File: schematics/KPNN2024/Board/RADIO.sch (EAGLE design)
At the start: 14 parts, among them J1 U.FL-R-SMT-1_10_, J2 U.FL-R-SMT-1_10_

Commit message: sdfghgfds
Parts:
- added C1: (no value), rcl:C-EUC0603
- added C2: ECAPECAP220, CanCubeSat:ECAPECAP220
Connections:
- net 3V3: no longer U$3.3.3V
- net 5V: now also C1.2, C2.1
- net GND: now also C1.1, C2.2
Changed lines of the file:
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@@
 <part name="R1" library="rcl" library_urn="urn:adsk.eagle:library:334" deviceset="R-US_" device="R0603" package3d_urn="urn:adsk.eagle:package:23555/3"/>
 <part name="R2" library="rcl" library_urn="urn:adsk.eagle:library:334" deviceset="R-US_" device="R0603" package3d_urn="urn:adsk.eagle:package:23555/3"/>
+<part name="C1" library="rcl" library_urn="urn:adsk.eagle:library:334" deviceset="C-EU" device="C0603" package3d_urn="urn:adsk.eagle:package:23616/2"/>
+<part name="C2" library="CanCubeSat" deviceset="ECAP" device="ECAP220"/>
 </parts>
 <sheets>
@@
 <attribute name="VALUE" x="143.51" y="83.058" size="1.778" layer="96"/>
 </instance>
+<instance part="C1" gate="G$1" x="53.34" y="83.82" smashed="yes">
+<attribute name="NAME" x="54.864" y="84.201" size="1.778" layer="95"/>
+<attribute name="VALUE" x="54.864" y="79.121" size="1.778" layer="96"/>
+</instance>
+<instance part="C2" gate="G$1" x="48.26" y="81.28" smashed="yes" rot="R180">
+<attribute name="NAME" x="47.244" y="80.645" size="1.778" layer="95" rot="R180"/>
+<attribute name="VALUE" x="47.244" y="85.471" size="1.778" layer="96" rot="R180"/>
+</instance>
 </instances>
 <busses>
@@
 <segment>
 <pinref part="U$3" gate="G$1" pin="GND"/>
-<wire x1="68.58" y1="83.82" x2="50.8" y2="83.82" width="0.1524" layer="91"/>
-<label x="50.8" y="83.82" size="1.778" layer="95"/>
+<wire x1="68.58" y1="83.82" x2="60.96" y2="83.82" width="0.1524" layer="91"/>
+<label x="55.88" y="86.36" size="1.778" layer="95"/>
+<pinref part="C1" gate="G$1" pin="1"/>
+<wire x1="53.34" y1="86.36" x2="60.96" y2="86.36" width="0.1524" layer="91"/>
+<wire x1="60.96" y1="86.36" x2="60.96" y2="83.82" width="0.1524" layer="91"/>
+<pinref part="C2" gate="G$1" pin="2"/>
+<wire x1="48.26" y1="86.36" x2="53.34" y2="86.36" width="0.1524" layer="91"/>
+<junction x="53.34" y="86.36"/>
 </segment>
 <segment>
@@
 </segment>
 <segment>
-<pinref part="U$3" gate="G$1" pin="3.3V"/>
-<wire x1="68.58" y1="73.66" x2="50.8" y2="73.66" width="0.1524" layer="91"/>
-<label x="50.8" y="73.66" size="1.778" layer="95"/>
-</segment>
-<segment>
 <pinref part="U$5" gate="G$1" pin="P$1"/>
 <wire x1="182.88" y1="83.82" x2="170.18" y2="83.82" width="0.1524" layer="91"/>
@@
 <segment>
 <pinref part="U$3" gate="G$1" pin="5V"/>
-<wire x1="68.58" y1="78.74" x2="50.8" y2="78.74" width="0.1524" layer="91"/>
-<label x="50.8" y="78.74" size="1.778" layer="95"/>
+<wire x1="68.58" y1="78.74" x2="53.34" y2="78.74" width="0.1524" layer="91"/>
+<label x="55.88" y="78.74" size="1.778" layer="95"/>
+<pinref part="C1" gate="G$1" pin="2"/>
+<pinref part="C2" gate="G$1" pin="1"/>
+<wire x1="48.26" y1="78.74" x2="53.34" y2="78.74" width="0.1524" layer="91"/>
+<junction x="53.34" y="78.74"/>
 </segment>
 <segment>

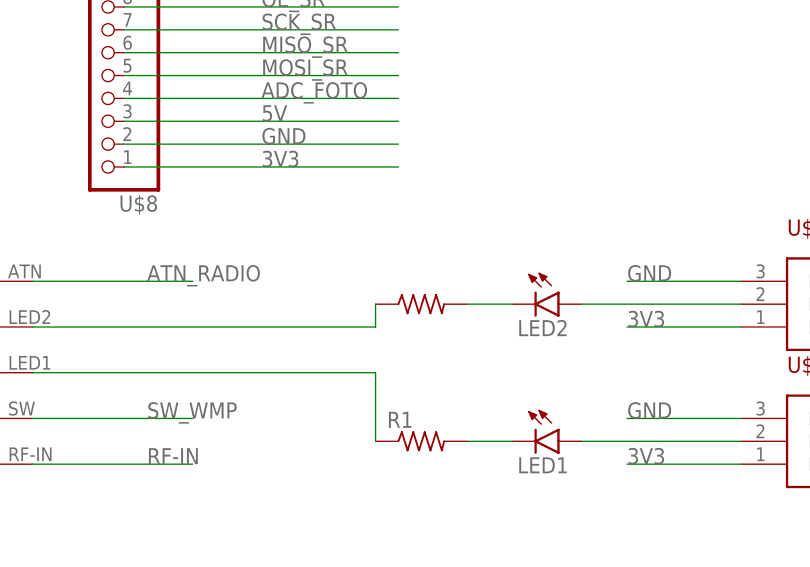
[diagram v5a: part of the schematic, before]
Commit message: добавлены стл корпусных деталей
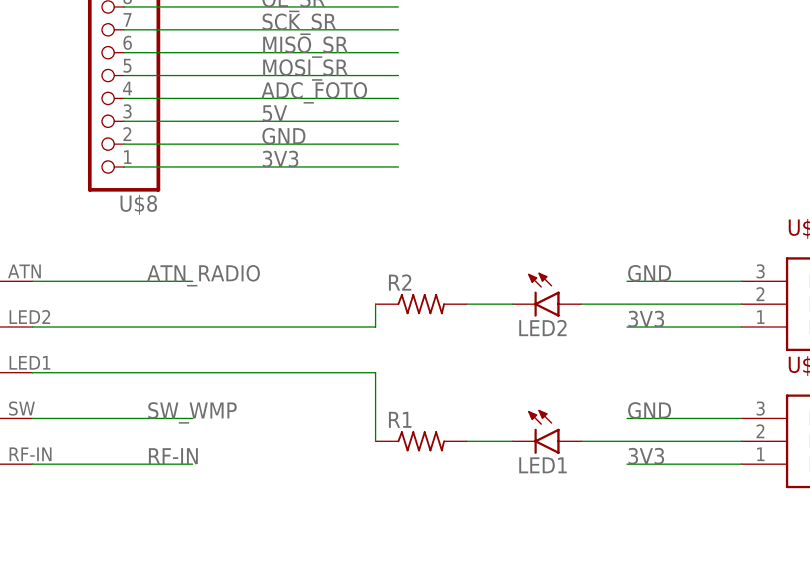
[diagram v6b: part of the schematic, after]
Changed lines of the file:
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@@
 <?xml version="1.0" encoding="utf-8"?>
 <!DOCTYPE eagle SYSTEM "eagle.dtd">
-<eagle version="9.6.0">
+<eagle version="9.6.2">
 <drawing>
 <settings>
@@
 </instance>
 <instance part="R2" gate="G$1" x="147.32" y="86.36" smashed="yes">
+<attribute name="NAME" x="143.51" y="87.8586" size="1.778" layer="95"/>
 <attribute name="VALUE" x="143.51" y="83.058" size="1.778" layer="96"/>
 </instance>

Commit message: ывавп лыл
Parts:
- C1: value (none) -> 100nF
- C2: value ECAPECAP220 -> 220uF
- J1: value U.FL-R-SMT-1_10_ -> IPX-RADIO
- J2: value U.FL-R-SMT-1_10_ -> IPX-ANT
- LED1: value (none) -> AMP1
- LED2: value (none) -> AMP2
- R1, R2: value (none) -> 2k
- renumbered U$1 to GPS-NEO7M, U$2 to NRF24LO1, U$3 to XQ-02A, U$4 to ROTATE1, U$5 to ROTATE2
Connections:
- net ATN_RADIO renamed ANT_RADIO

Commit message: Платы вроде готовы
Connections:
- net DIR_DRIVER: now also U$6.2, U$8.12; no longer U$6.1, U$8.13
- net STEP_DRIVER: now also U$6.1, U$8.13; no longer U$6.2, U$8.12
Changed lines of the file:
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@@
 <?xml version="1.0" encoding="utf-8"?>
 <!DOCTYPE eagle SYSTEM "eagle.dtd">
-<eagle version="9.6.2">
+<eagle version="9.4.2">
 <drawing>
 <settings>
-<setting alwaysvectorfont="no"/>
+<setting alwaysvectorfont="yes"/>
 <setting verticaltext="up"/>
 </settings>
@@
 <net name="DIR_DRIVER" class="0">
 <segment>
+<pinref part="U$6" gate="G$1" pin="2"/>
+<wire x1="40.64" y1="129.54" x2="10.16" y2="129.54" width="0.1524" layer="91"/>
+<label x="10.16" y="129.54" size="1.778" layer="95"/>
+</segment>
+<segment>
+<wire x1="144.78" y1="129.54" x2="114.3" y2="129.54" width="0.1524" layer="91"/>
+<label x="129.54" y="129.54" size="1.778" layer="95"/>
+<pinref part="U$8" gate="G$1" pin="12"/>
+</segment>
+</net>
+<net name="STEP_DRIVER" class="0">
+<segment>
 <pinref part="U$6" gate="G$1" pin="1"/>
 <wire x1="40.64" y1="132.08" x2="10.16" y2="132.08" width="0.1524" layer="91"/>
@@
 </segment>
 </net>
-<net name="STEP_DRIVER" class="0">
-<segment>
-<pinref part="U$6" gate="G$1" pin="2"/>
-<wire x1="40.64" y1="129.54" x2="10.16" y2="129.54" width="0.1524" layer="91"/>
-<label x="10.16" y="129.54" size="1.778" layer="95"/>
-</segment>
-<segment>
-<wire x1="144.78" y1="129.54" x2="114.3" y2="129.54" width="0.1524" layer="91"/>
-<label x="129.54" y="129.54" size="1.778" layer="95"/>
-<pinref part="U$8" gate="G$1" pin="12"/>
-</segment>
-</net>
